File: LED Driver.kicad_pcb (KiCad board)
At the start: 2 copper layers, 15 x 15 mm, 9 parts, among them J1 CONN_01X02, J2 CONN_01X03, J3 GS3, U1 AP5724

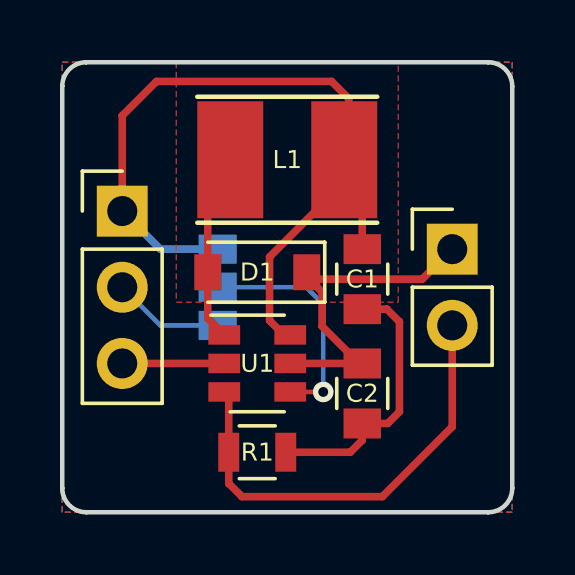
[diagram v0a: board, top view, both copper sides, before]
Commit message: Adds labels to silkscreen (copied from NCP5006 branch)
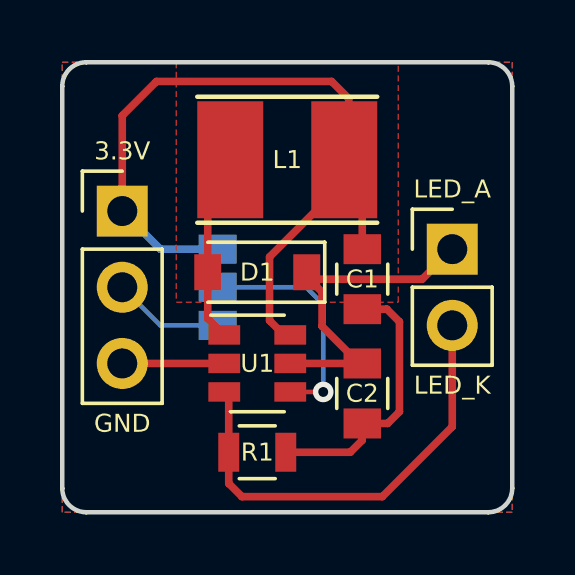
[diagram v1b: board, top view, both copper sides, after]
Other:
- board text added: "3.3V"
- board text added: "EN"
- board text added: "EN_CONN"
- board text added: "GND"
- board text added: "LED_A"
- board text added: "LED_K"
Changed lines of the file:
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@@
     (area 99.924999 84.924999 115.075001 100.075001)
     (thickness 1.6)
-    (drawings 8)
+    (drawings 15)
     (tracks 52)
     (zones 0)
@@
       (net 6 /EN_CONN))
   )
+  (gr_text EN_CONN (at 106.2 93.77) (layer B.SilkS)
+    (effects (font (size 0.6 0.6) (thickness 0.15)) (justify right mirror))
+  )
+  (gr_text EN (at 106.2 92.5) (layer B.SilkS)
+    (effects (font (size 0.6 0.6) (thickness 0.15)) (justify right mirror))
+  )
+  (gr_text 3.3V (at 106.2 91.23) (layer B.SilkS)
+    (effects (font (size 0.6 0.6) (thickness 0.15)) (justify right mirror))
+  )
+  (gr_text GND (at 102 97.04) (layer F.SilkS)
+    (effects (font (size 0.6 0.6) (thickness 0.15)))
+  )
+  (gr_text 3.3V (at 102 87.96) (layer F.SilkS)
+    (effects (font (size 0.6 0.6) (thickness 0.15)))
+  )
+  (gr_text LED_K (at 113 95.77) (layer F.SilkS)
+    (effects (font (size 0.6 0.6) (thickness 0.15)))
+  )
+  (gr_text LED_A (at 113 89.23) (layer F.SilkS)
+    (effects (font (size 0.6 0.6) (thickness 0.15)))
+  )
   (gr_arc (start 114.2 99.2) (end 115 99.2) (angle 90) (layer Edge.Cuts) (width 0.15))

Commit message: Adds project name and version (v1.0) to silkscreen
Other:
- board text added: "LED Driver - AP5724"
- board text added: "v1.0"
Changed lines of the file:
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@@
     (area 99.924999 84.924999 115.075001 100.075001)
     (thickness 1.6)
-    (drawings 15)
+    (drawings 17)
     (tracks 52)
     (zones 0)
@@
       (net 6 /EN_CONN))
   )
+  (gr_text v1.0 (at 102 98) (layer B.SilkS)
+    (effects (font (size 0.8 0.8) (thickness 0.18)) (justify mirror))
+  )
+  (gr_text "LED Driver - AP5724" (at 107.5 87.25) (layer B.SilkS)
+    (effects (font (size 0.8 0.8) (thickness 0.18)) (justify mirror))
+  )
   (gr_text EN_CONN (at 106.2 93.77) (layer B.SilkS)
